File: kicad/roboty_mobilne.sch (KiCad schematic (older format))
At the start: 20 parts, among them J2 ST-Link Pin, J3 UART Debug, SW3 SW_Push, SW4 SW_Push, U6 YAAJ_BluePill_Part_Like

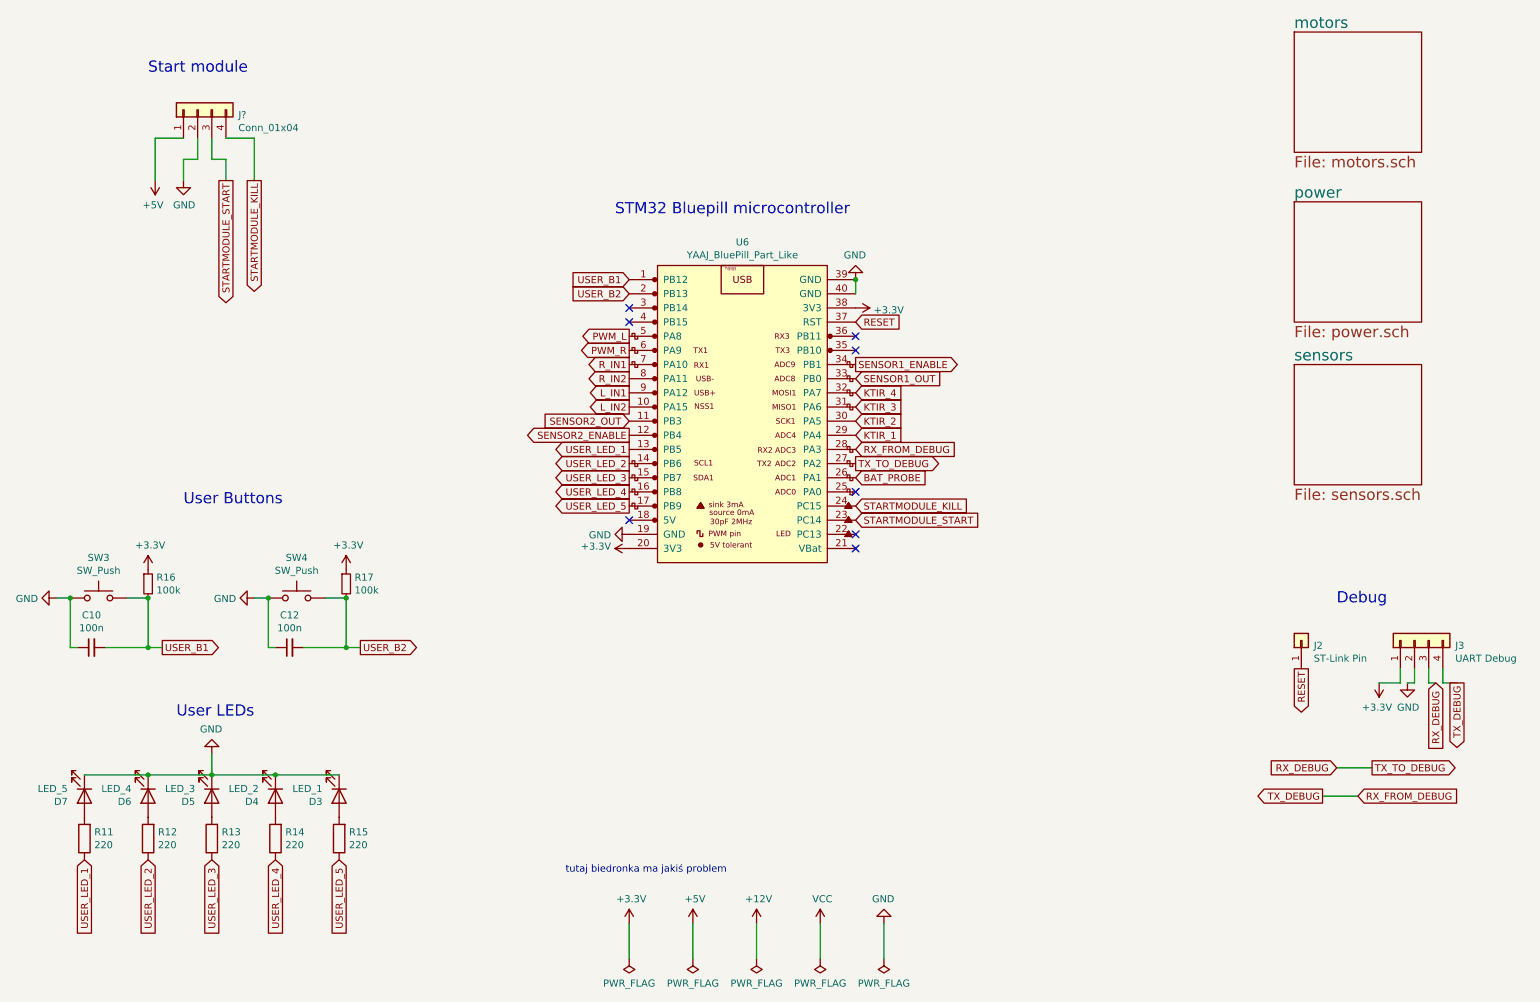
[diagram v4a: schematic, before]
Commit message: deleted 3.3V and modified everything to use 5V instead
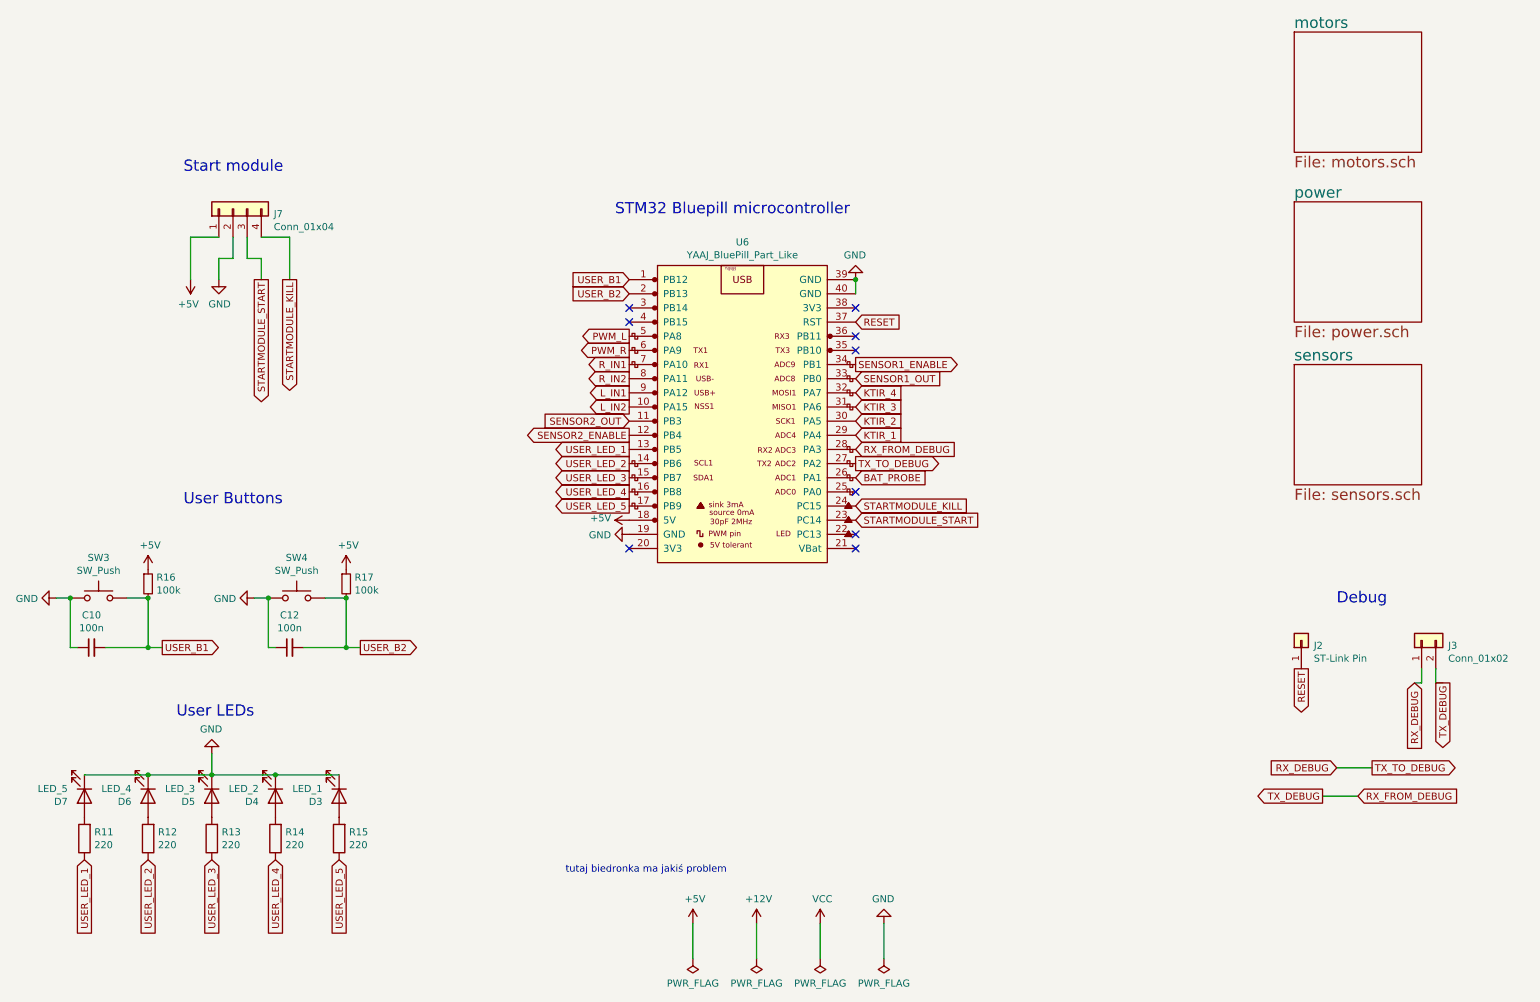
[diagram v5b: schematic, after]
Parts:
- removed J3: UART Debug, symbol Connector_Generic:Conn_01x04
- added J3: Conn_01x02, Connector_PinSocket_2.54mm:PinSocket_1x02_P2.54mm_Vertical, symbol Connector_Generic:Conn_01x02
- D3, D4, D5, D6, D7: footprint (none) -> LED_THT:LED_D5.0mm
- J2: footprint (none) -> Connector_PinSocket_2.54mm:PinSocket_1x01_P2.54mm_Vertical
- J7: renamed from J?; footprint (none) -> Connector_PinSocket_2.54mm:PinSocket_1x04_P2.54mm_Vertical
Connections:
- net +5V: now also R16.1, R17.1, U6.18 (5V)
- net RX_DEBUG: now also J3.1 (Pin_1)
- net RX_FROM_DEBUG: now also J3.2 (Pin_2)
- removed net +3V3: R16.1, R17.1, U6.20 (3V3), U6.38 (3V3)
- no-connect marks 8 -> 9
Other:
- moved on the sheet: J7
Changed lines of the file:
@@
 F 0 "J2" V 9564 5112 50  0000 R CNN
 F 1 "ST-Link Pin" V 9473 5112 50  0000 R CNN
-F 2 "" H 9600 5200 50  0001 C CNN
+F 2 "Connector_PinSocket_2.54mm:PinSocket_1x01_P2.54mm_Vertical" H 9600 5200 50  0001 C CNN
 F 3 "~" H 9600 5200 50  0001 C CNN
 	1    9600 5200
@@
 Wire Wire Line
 	6200 7200 6200 7450
-$Comp
-L Connector_Generic:Conn_01x04 J3
-U 1 1 60A36A04
-P 10400 5200
-F 0 "J3" V 10364 4912 50  0000 R CNN
-F 1 "UART Debug" V 10273 4912 50  0000 R CNN
-F 2 "" H 10400 5200 50  0001 C CNN
-F 3 "~" H 10400 5200 50  0001 C CNN
-	1    10400 5200
-	0    -1   -1   0
-$EndComp
-$Comp
-L power:+3.3V #PWR019
-U 1 1 60A38B1A
-P 10150 5500
-F 0 "#PWR019" H 10150 5350 50  0001 C CNN
-F 1 "+3.3V" H 10165 5673 50  0000 C CNN
-F 2 "" H 10150 5500 50  0001 C CNN
-F 3 "" H 10150 5500 50  0001 C CNN
-	1    10150 5500
-	-1   0    0    1
-$EndComp
-$Comp
-L power:GND #PWR020
-U 1 1 60A3A18F
-P 10350 5500
-F 0 "#PWR020" H 10350 5250 50  0001 C CNN
-F 1 "GND" H 10355 5327 50  0000 C CNN
-F 2 "" H 10350 5500 50  0001 C CNN
-F 3 "" H 10350 5500 50  0001 C CNN
-	1    10350 5500
-	1    0    0    -1
-$EndComp
-Text GLabel 10550 5500 3    50   Input ~ 0
+Text GLabel 10400 5500 3    50   Input ~ 0
 RX_DEBUG
 Text GLabel 9850 6100 0    50   Input ~ 0
@@
 Text GLabel 10100 6100 2    50   Output ~ 0
 TX_TO_DEBUG
-Text GLabel 10700 5500 3    50   Output ~ 0
+Text GLabel 10600 5500 3    50   Output ~ 0
 TX_DEBUG
 Text GLabel 9750 6300 0    50   Output ~ 0
@@
 	1    0    0    -1
 $EndComp
-$Comp
-L power:+3.3V #PWR030
-U 1 1 60A870C4
-P 1450 4700
-F 0 "#PWR030" H 1450 4550 50  0001 C CNN
-F 1 "+3.3V" H 1465 4873 50  0000 C CNN
-F 2 "" H 1450 4700 50  0001 C CNN
-F 3 "" H 1450 4700 50  0001 C CNN
-	1    1450 4700
-	1    0    0    -1
-$EndComp
 Wire Wire Line
 	800  4900 900  4900
@@
 F 3 "~" H 2850 4800 50  0001 C CNN
 	1    2850 4800
-	1    0    0    -1
-$EndComp
-$Comp
-L power:+3.3V #PWR035
-U 1 1 60AA8745
-P 2850 4700
-F 0 "#PWR035" H 2850 4550 50  0001 C CNN
-F 1 "+3.3V" H 2865 4873 50  0000 C CNN
-F 2 "" H 2850 4700 50  0001 C CNN
-F 3 "" H 2850 4700 50  0001 C CNN
-	1    2850 4700
 	1    0    0    -1
 $EndComp
@@
 	-1   0    0    1
 $EndComp
-Wire Wire Line
-	10300 5400 10300 5500
-Wire Wire Line
-	10300 5500 10150 5500
-Wire Wire Line
-	10350 5500 10400 5500
-Wire Wire Line
-	10400 5500 10400 5400
-Wire Wire Line
-	10550 5500 10500 5500
-Wire Wire Line
-	10500 5500 10500 5400
-Wire Wire Line
-	10700 5500 10600 5500
-Wire Wire Line
-	10600 5500 10600 5400
 $Comp
 L power:PWR_FLAG #FLG0101
@@
 Wire Wire Line
 	5300 7200 5300 7450
-$Comp
-L power:+3.3V #PWR0102
-U 1 1 60AEF2CB
-P 4850 7200
-F 0 "#PWR0102" H 4850 7050 50  0001 C CNN
-F 1 "+3.3V" H 4865 7373 50  0000 C CNN
-F 2 "" H 4850 7200 50  0001 C CNN
-F 3 "" H 4850 7200 50  0001 C CNN
-	1    4850 7200
-	1    0    0    -1
-$EndComp
-$Comp
-L power:PWR_FLAG #FLG0104
-U 1 1 60AEF2D1
-P 4850 7450
-F 0 "#FLG0104" H 4850 7525 50  0001 C CNN
-F 1 "PWR_FLAG" H 4850 7623 50  0000 C CNN
-F 2 "" H 4850 7450 50  0001 C CNN
-F 3 "~" H 4850 7450 50  0001 C CNN
-	1    4850 7450
-	-1   0    0    1
-$EndComp
-Wire Wire Line
-	4850 7200 4850 7450
 $Comp
 L power:+12V #PWR0103
@@
 $EndComp
 $Comp
-L power:+3.3V #PWR017
-U 1 1 60A44804
-P 4850 4550
-F 0 "#PWR017" H 4850 4400 50  0001 C CNN
-F 1 "+3.3V" V 4865 4678 50  0000 L CNN
-F 2 "" H 4850 4550 50  0001 C CNN
-F 3 "" H 4850 4550 50  0001 C CNN
-	1    4850 4550
-	0    -1   -1   0
-$EndComp
-$Comp
 L power:GND #PWR024
 U 1 1 60A45AC6
@@
 	6450 2750 6450 2650
 Connection ~ 6450 2650
-$Comp
-L power:+3.3V #PWR025
-U 1 1 60A48A3A
-P 6450 2850
-F 0 "#PWR025" H 6450 2700 50  0001 C CNN
-F 1 "+3.3V" V 6465 2978 50  0000 L CNN
-F 2 "" H 6450 2850 50  0001 C CNN
-F 3 "" H 6450 2850 50  0001 C CNN
-	1    6450 2850
-	0    1    1    0
-$EndComp
 Text GLabel 4850 3650 0    50   Input ~ 0
 SENSOR2_OUT
@@
 NoConn ~ 6450 4450
 NoConn ~ 6450 4150
-NoConn ~ 4850 4350
 NoConn ~ 4850 2950
 NoConn ~ 4850 2850
@@
 F 0 "D7" V 1039 6182 50  0000 R CNN
 F 1 "LED_5" V 948 6182 50  0000 R CNN
-F 2 "" H 1000 6300 50  0001 C CNN
+F 2 "LED_THT:LED_D5.0mm" H 1000 6300 50  0001 C CNN
 F 3 "~" H 1000 6300 50  0001 C CNN
 	1    1000 6300
@@
 F 0 "D6" V 1489 6182 50  0000 R CNN
 F 1 "LED_4" V 1398 6182 50  0000 R CNN
-F 2 "" H 1450 6300 50  0001 C CNN
+F 2 "LED_THT:LED_D5.0mm" H 1450 6300 50  0001 C CNN
 F 3 "~" H 1450 6300 50  0001 C CNN
 	1    1450 6300
@@
 F 0 "D5" V 1939 6182 50  0000 R CNN
 F 1 "LED_3" V 1848 6182 50  0000 R CNN
-F 2 "" H 1900 6300 50  0001 C CNN
+F 2 "LED_THT:LED_D5.0mm" H 1900 6300 50  0001 C CNN
 F 3 "~" H 1900 6300 50  0001 C CNN
 	1    1900 6300
@@
 F 0 "D4" V 2389 6182 50  0000 R CNN
 F 1 "LED_2" V 2298 6182 50  0000 R CNN
-F 2 "" H 2350 6300 50  0001 C CNN
+F 2 "LED_THT:LED_D5.0mm" H 2350 6300 50  0001 C CNN
 F 3 "~" H 2350 6300 50  0001 C CNN
 	1    2350 6300
@@
 F 0 "D3" V 2839 6182 50  0000 R CNN
 F 1 "LED_1" V 2748 6182 50  0000 R CNN
-F 2 "" H 2800 6300 50  0001 C CNN
+F 2 "LED_THT:LED_D5.0mm" H 2800 6300 50  0001 C CNN
 F 3 "~" H 2800 6300 50  0001 C CNN
 	1    2800 6300
@@
 $EndComp
 $Comp
-L power:GND #PWR?
+L power:GND #PWR0101
 U 1 1 60BF95BC
 P 1900 6000
-F 0 "#PWR?" H 1900 5750 50  0001 C CNN
+F 0 "#PWR0101" H 1900 5750 50  0001 C CNN
 F 1 "GND" H 1905 5827 50  0000 C CNN
 F 2 "" H 1900 6000 50  0001 C CNN
@@
 Text GLabel 6450 4250 2    50   Input ~ 0
 STARTMODULE_KILL
-Text Notes 1450 1200 0    79   ~ 0
+Text Notes 1700 1900 0    79   ~ 0
 Start module
 $Comp
-L Connector_Generic:Conn_01x04 J?
+L Connector_Generic:Conn_01x04 J7
 U 1 1 60C0AD19
-P 1800 1450
-F 0 "J?" V 1764 1162 50  0000 R CNN
-F 1 "Conn_01x04" V 1673 1162 50  0000 R CNN
-F 2 "" H 1800 1450 50  0001 C CNN
-F 3 "~" H 1800 1450 50  0001 C CNN
-	1    1800 1450
+P 2050 2150
+F 0 "J7" V 2014 1862 50  0000 R CNN
+F 1 "Conn_01x04" V 1923 1862 50  0000 R CNN
+F 2 "Connector_PinSocket_2.54mm:PinSocket_1x04_P2.54mm_Vertical" H 2050 2150 50  0001 C CNN
+F 3 "~" H 2050 2150 50  0001 C CNN
+	1    2050 2150
 	0    -1   -1   0
 $EndComp
 $Comp
-L power:+5V #PWR?
+L power:+5V #PWR0102
 U 1 1 60C0B99A
-P 1500 1950
-F 0 "#PWR?" H 1500 1800 50  0001 C CNN
-F 1 "+5V" H 1515 2123 50  0000 C CNN
-F 2 "" H 1500 1950 50  0001 C CNN
-F 3 "" H 1500 1950 50  0001 C CNN
-	1    1500 1950
-	-1   0    0    1
-$EndComp
-$Comp
-L power:GND #PWR?
+P 1750 2650
+F 0 "#PWR0102" H 1750 2500 50  0001 C CNN
+F 1 "+5V" H 1765 2823 50  0000 C CNN
+F 2 "" H 1750 2650 50  0001 C CNN
+F 3 "" H 1750 2650 50  0001 C CNN
+	1    1750 2650
+	-1   0    0    1
+$EndComp
+$Comp
+L power:GND #PWR0108
 U 1 1 60C0DD49
-P 1700 1950
-F 0 "#PWR?" H 1700 1700 50  0001 C CNN
-F 1 "GND" H 1705 1777 50  0000 C CNN
-F 2 "" H 1700 1950 50  0001 C CNN
-F 3 "" H 1700 1950 50  0001 C CNN
-	1    1700 1950
-	1    0    0    -1
-$EndComp
-Text GLabel 2000 1950 3    50   Output ~ 0
+P 1950 2650
+F 0 "#PWR0108" H 1950 2400 50  0001 C CNN
+F 1 "GND" H 1955 2477 50  0000 C CNN
+F 2 "" H 1950 2650 50  0001 C CNN
+F 3 "" H 1950 2650 50  0001 C CNN
+	1    1950 2650
+	1    0    0    -1
+$EndComp
+Text GLabel 2250 2650 3    50   Output ~ 0
 STARTMODULE_START
-Text GLabel 2200 1950 3    50   Output ~ 0
+Text GLabel 2450 2650 3    50   Output ~ 0
 STARTMODULE_KILL
 Wire Wire Line
-	2000 1650 2200 1650
-Wire Wire Line
-	2200 1650 2200 1950
-Wire Wire Line
-	1700 1650 1500 1650
-Wire Wire Line
-	1500 1650 1500 1950
-Wire Wire Line
-	1700 1950 1700 1800
-Wire Wire Line
-	1700 1800 1800 1800
-Wire Wire Line
-	1800 1800 1800 1650
-Wire Wire Line
-	2000 1950 2000 1800
-Wire Wire Line
-	2000 1800 1900 1800
-Wire Wire Line
-	1900 1800 1900 1650
+	2250 2350 2450 2350
+Wire Wire Line
+	2450 2350 2450 2650
+Wire Wire Line
+	1950 2350 1750 2350
+Wire Wire Line
+	1750 2350 1750 2650
+Wire Wire Line
+	1950 2650 1950 2500
+Wire Wire Line
+	1950 2500 2050 2500
+Wire Wire Line
+	2050 2500 2050 2350
+Wire Wire Line
+	2250 2650 2250 2500
+Wire Wire Line
+	2250 2500 2150 2500
+Wire Wire Line
+	2150 2500 2150 2350
 Text GLabel 6450 4050 2    50   Input ~ 0
 BAT_PROBE
+$Comp
+L power:+5V #PWR0112
+U 1 1 60BCEF3D
+P 2850 4700
+F 0 "#PWR0112" H 2850 4550 50  0001 C CNN
+F 1 "+5V" H 2865 4873 50  0000 C CNN
+F 2 "" H 2850 4700 50  0001 C CNN
+F 3 "" H 2850 4700 50  0001 C CNN
+	1    2850 4700
+	1    0    0    -1
+$EndComp
+$Comp
+L power:+5V #PWR0124
+U 1 1 60BD11BF
+P 1450 4700
+F 0 "#PWR0124" H 1450 4550 50  0001 C CNN
+F 1 "+5V" H 1465 4873 50  0000 C CNN
+F 2 "" H 1450 4700 50  0001 C CNN
+F 3 "" H 1450 4700 50  0001 C CNN
+	1    1450 4700
+	1    0    0    -1
+$EndComp
+NoConn ~ 4850 4550
+$Comp
+L power:+5V #PWR0125
+U 1 1 60BD57B1
+P 4850 4350
+F 0 "#PWR0125" H 4850 4200 50  0001 C CNN
+F 1 "+5V" V 4865 4478 50  0000 L CNN
+F 2 "" H 4850 4350 50  0001 C CNN
+F 3 "" H 4850 4350 50  0001 C CNN
+	1    4850 4350
+	0    -1   -1   0
+$EndComp
+NoConn ~ 6450 2850
+$Comp
+L Connector_Generic:Conn_01x02 J3
+U 1 1 60BE7053
+P 10450 5200
+F 0 "J3" V 10414 5012 50  0000 R CNN
+F 1 "Conn_01x02" V 10323 5012 50  0000 R CNN
+F 2 "Connector_PinSocket_2.54mm:PinSocket_1x02_P2.54mm_Vertical" H 10450 5200 50  0001 C CNN
+F 3 "~" H 10450 5200 50  0001 C CNN
+	1    10450 5200
+	0    -1   -1   0
+$EndComp
+Wire Wire Line
+	10450 5400 10450 5500
+Wire Wire Line
+	10450 5500 10400 5500
+Wire Wire Line
+	10550 5400 10550 5500
+Wire Wire Line
+	10550 5500 10600 5500
 $EndSCHEMATC

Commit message: created pcb view
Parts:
- C10, C12: value 100n -> 0.1u; footprint (none) -> Capacitor_THT:C_Disc_D10.5mm_W5.0mm_P7.50mm
- R11, R12, R13, R14, R15: value 220 -> 330; footprint (none) -> Resistor_SMD:R_1206_3216Metric_Pad1.30x1.75mm_HandSolder
- R16, R17: footprint (none) -> Resistor_SMD:R_1206_3216Metric_Pad1.30x1.75mm_HandSolder
- SW3, SW4: footprint (none) -> Button_Switch_THT:SW_PUSH_6mm_H5mm
- U6: footprint (none) -> bluepill:YAAJ_BluePill_1
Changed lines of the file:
@@
 F 0 "SW3" H 1100 5185 50  0000 C CNN
 F 1 "SW_Push" H 1100 5094 50  0000 C CNN
-F 2 "" H 1100 5100 50  0001 C CNN
+F 2 "Button_Switch_THT:SW_PUSH_6mm_H5mm" H 1100 5100 50  0001 C CNN
 F 3 "~" H 1100 5100 50  0001 C CNN
 	1    1100 4900
@@
 P 1050 5250
 F 0 "C10" V 1279 5250 50  0000 C CNN
-F 1 "100n" V 1188 5250 50  0000 C CNN
-F 2 "" H 1050 5250 50  0001 C CNN
+F 1 "0.1u" V 1188 5250 50  0000 C CNN
+F 2 "Capacitor_THT:C_Disc_D10.5mm_W5.0mm_P7.50mm" H 1050 5250 50  0001 C CNN
 F 3 "~" H 1050 5250 50  0001 C CNN
 	1    1050 5250
@@
 F 0 "R16" H 1509 4846 50  0000 L CNN
 F 1 "100k" H 1509 4755 50  0000 L CNN
-F 2 "" H 1450 4800 50  0001 C CNN
+F 2 "Resistor_SMD:R_1206_3216Metric_Pad1.30x1.75mm_HandSolder" H 1450 4800 50  0001 C CNN
 F 3 "~" H 1450 4800 50  0001 C CNN
 	1    1450 4800
@@
 F 0 "SW4" H 2500 5185 50  0000 C CNN
 F 1 "SW_Push" H 2500 5094 50  0000 C CNN
-F 2 "" H 2500 5100 50  0001 C CNN
+F 2 "Button_Switch_THT:SW_PUSH_6mm_H5mm" H 2500 5100 50  0001 C CNN
 F 3 "~" H 2500 5100 50  0001 C CNN
 	1    2500 4900
@@
 F 0 "R17" H 2909 4846 50  0000 L CNN
 F 1 "100k" H 2909 4755 50  0000 L CNN
-F 2 "" H 2850 4800 50  0001 C CNN
+F 2 "Resistor_SMD:R_1206_3216Metric_Pad1.30x1.75mm_HandSolder" H 2850 4800 50  0001 C CNN
 F 3 "~" H 2850 4800 50  0001 C CNN
 	1    2850 4800
@@
 P 2450 5250
 F 0 "C12" V 2679 5250 50  0000 C CNN
-F 1 "100n" V 2588 5250 50  0000 C CNN
-F 2 "" H 2450 5250 50  0001 C CNN
+F 1 "0.1u" V 2588 5250 50  0000 C CNN
+F 2 "Capacitor_THT:C_Disc_D10.5mm_W5.0mm_P7.50mm" H 2450 5250 50  0001 C CNN
 F 3 "~" H 2450 5250 50  0001 C CNN
 	1    2450 5250
@@
 P 2800 6600
 F 0 "R15" H 2730 6554 50  0000 R CNN
-F 1 "220" H 2730 6645 50  0000 R CNN
-F 2 "" V 2730 6600 50  0001 C CNN
+F 1 "330" H 2730 6645 50  0000 R CNN
+F 2 "Resistor_SMD:R_1206_3216Metric_Pad1.30x1.75mm_HandSolder" V 2730 6600 50  0001 C CNN
 F 3 "~" H 2800 6600 50  0001 C CNN
 	1    2800 6600
@@
 P 2350 6600
 F 0 "R14" H 2280 6554 50  0000 R CNN
-F 1 "220" H 2280 6645 50  0000 R CNN
-F 2 "" V 2280 6600 50  0001 C CNN
+F 1 "330" H 2280 6645 50  0000 R CNN
+F 2 "Resistor_SMD:R_1206_3216Metric_Pad1.30x1.75mm_HandSolder" V 2280 6600 50  0001 C CNN
 F 3 "~" H 2350 6600 50  0001 C CNN
 	1    2350 6600
@@
 P 1900 6600
 F 0 "R13" H 1830 6554 50  0000 R CNN
-F 1 "220" H 1830 6645 50  0000 R CNN
-F 2 "" V 1830 6600 50  0001 C CNN
+F 1 "330" H 1830 6645 50  0000 R CNN
+F 2 "Resistor_SMD:R_1206_3216Metric_Pad1.30x1.75mm_HandSolder" V 1830 6600 50  0001 C CNN
 F 3 "~" H 1900 6600 50  0001 C CNN
 	1    1900 6600
@@
 P 1450 6600
 F 0 "R12" H 1380 6554 50  0000 R CNN
-F 1 "220" H 1380 6645 50  0000 R CNN
-F 2 "" V 1380 6600 50  0001 C CNN
+F 1 "330" H 1380 6645 50  0000 R CNN
+F 2 "Resistor_SMD:R_1206_3216Metric_Pad1.30x1.75mm_HandSolder" V 1380 6600 50  0001 C CNN
 F 3 "~" H 1450 6600 50  0001 C CNN
 	1    1450 6600
@@
 P 1000 6600
 F 0 "R11" H 930 6554 50  0000 R CNN
-F 1 "220" H 930 6645 50  0000 R CNN
-F 2 "" V 930 6600 50  0001 C CNN
+F 1 "330" H 930 6645 50  0000 R CNN
+F 2 "Resistor_SMD:R_1206_3216Metric_Pad1.30x1.75mm_HandSolder" V 930 6600 50  0001 C CNN
 F 3 "~" H 1000 6600 50  0001 C CNN
 	1    1000 6600
@@
 F 0 "U6" H 5650 4715 50  0000 C CNN
 F 1 "YAAJ_BluePill_Part_Like" H 5650 4624 50  0000 C CNN
-F 2 "" H 6350 2550 50  0001 C CNN
+F 2 "bluepill:YAAJ_BluePill_1" H 6350 2550 50  0001 C CNN
 F 3 "" H 6350 2550 50  0001 C CNN
 	1    5650 3550
